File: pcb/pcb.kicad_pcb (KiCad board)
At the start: 2 copper layers, 61.6 x 63.7 mm, 7 parts, among them J1 Conn_01x02

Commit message: Reroute, repour
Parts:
- D1: footprint LED_SMD:LED_0805_2012Metric_Pad1.15x1.40mm_HandSolder -> pcb:universal_LED
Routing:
- net GND: track 144.9 -> 15.2 mm
- net +5V: track 131.2 -> 127.9 mm

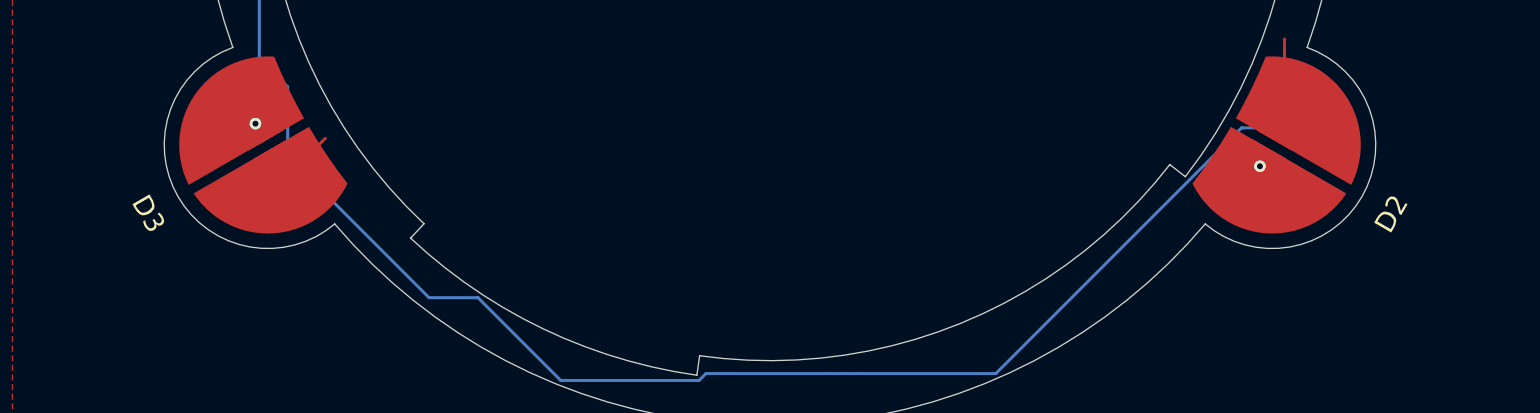
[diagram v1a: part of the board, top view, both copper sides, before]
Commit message: Update capitalization
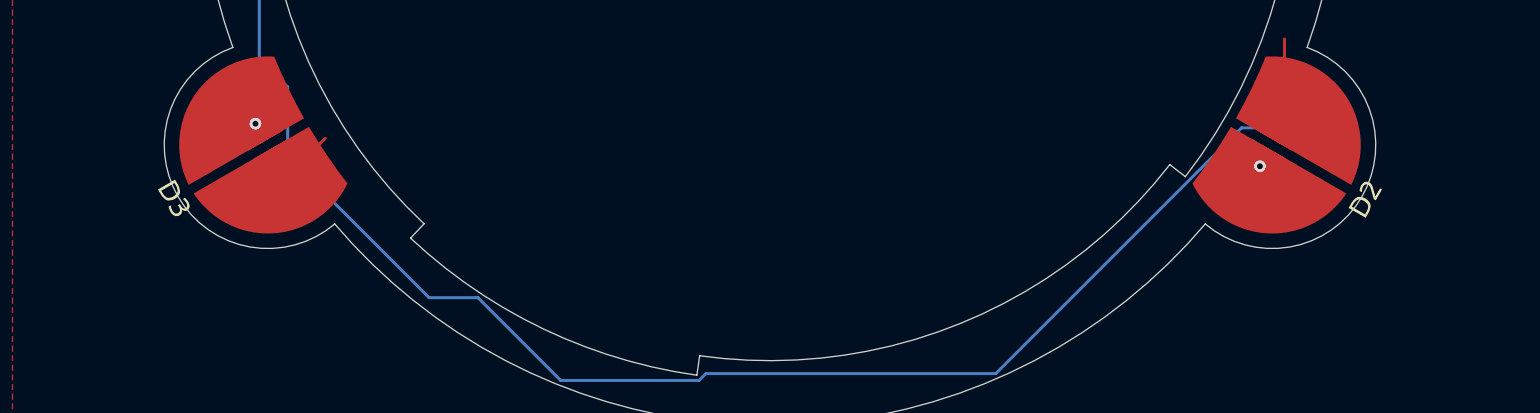
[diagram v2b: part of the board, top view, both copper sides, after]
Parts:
- D1, D2, D3: footprint pcb:universal_LED -> pcb:Universal_LED

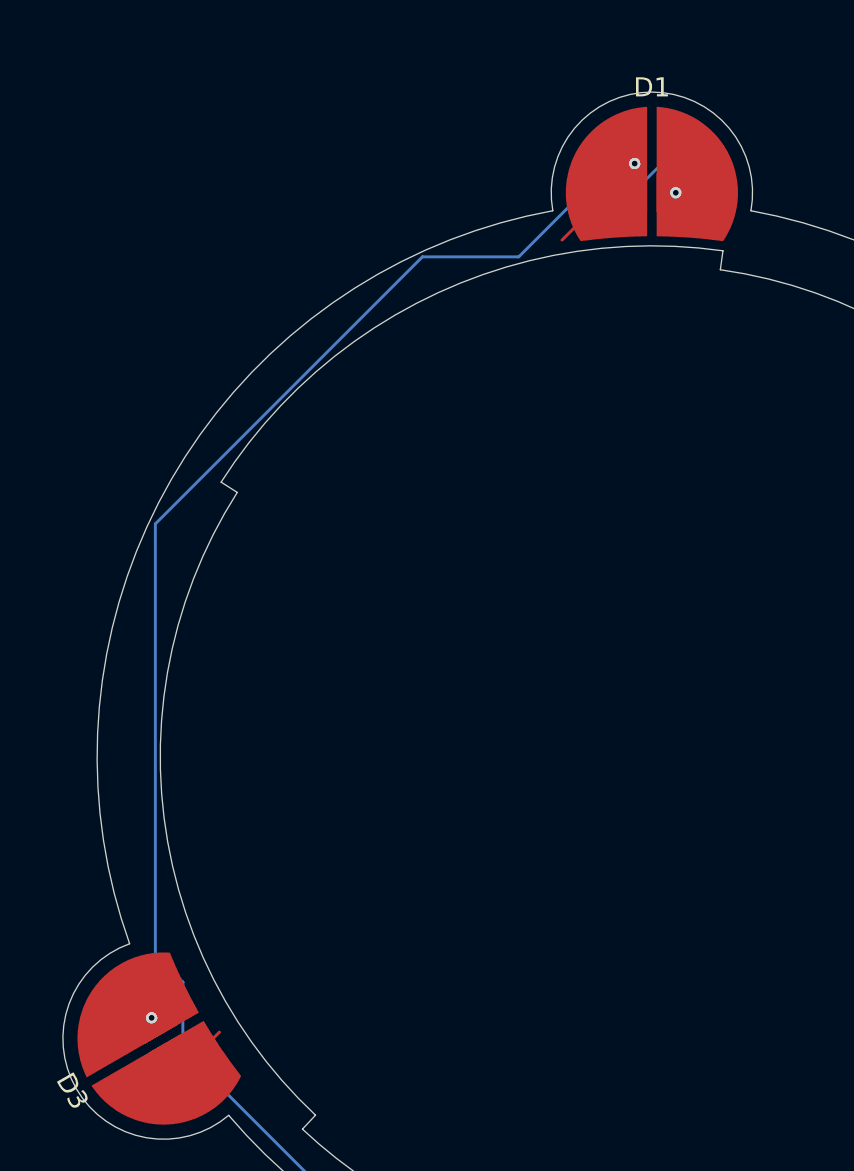
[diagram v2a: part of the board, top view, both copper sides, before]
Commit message: Use new power connection
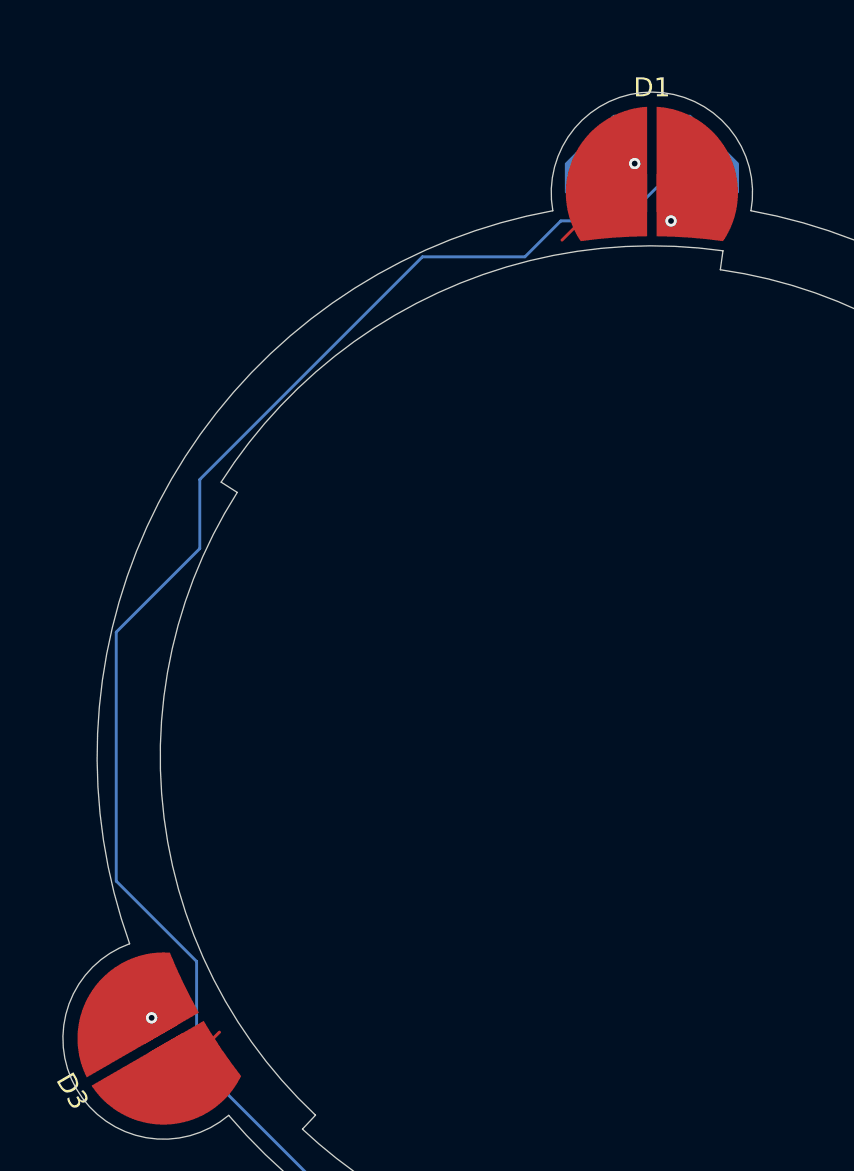
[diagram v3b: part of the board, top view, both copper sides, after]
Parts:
- J1: footprint Resistor_SMD:R_0805_2012Metric_Pad1.20x1.40mm_HandSolder -> pcb:Power_Connection
- moved J1 3.00 mm to (148.5, 75.5), turned to 180 degrees
- moved R1 1.47 mm to (148.5, 77.0)
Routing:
- net Net-(D1-Pad2): track 0.25 -> 1.80 mm
- net +5V: track 127.9 -> 129.1 mm
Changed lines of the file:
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@@
     (thickness 1.6)
     (drawings 18)
-    (tracks 38)
+    (tracks 42)
     (zones 0)
     (modules 7)
@@
     (38 B.Mask user hide)
     (39 F.Mask user hide)
-    (40 Dwgs.User user hide)
+    (40 Dwgs.User user)
     (41 Cmts.User user hide)
     (42 Eco1.User user hide)
@@
   )
   (module Resistor_SMD:R_0805_2012Metric_Pad1.20x1.40mm_HandSolder (layer B.Cu)
-    (at 148.5 72.5)
-    (descr "Resistor SMD 0805 (2012 Metric), square (rectangular) end terminal, IPC_7351 nominal with elongated pad for handsoldering. (Body size source: IPC-SM-782 page 72, https://www.pcb-3d.com/wordpress/wp-content/uploads/ipc-sm-782a_amendment_1_and_2.pdf), generated with kicad-footprint-generator")
-    (tags "resistor handsolder")
-    (attr smd)
-    (fp_text reference J1 (at 0 1.65 180) (layer B.SilkS)
-      (effects (font (size 1 1) (thickness 0.15)) (justify mirror))
-    )
-    (fp_text value Conn_01x02 (at 0 -1.65 180) (layer B.Fab)
-      (effects (font (size 1 1) (thickness 0.15)) (justify mirror))
-    )
-    (fp_text user %R (at 0 0 180) (layer B.Fab)
-      (effects (font (size 0.5 0.5) (thickness 0.08)) (justify mirror))
-    )
-    (fp_line (start -1 -0.625) (end -1 0.625) (layer B.Fab) (width 0.1))
-    (fp_line (start -1 0.625) (end 1 0.625) (layer B.Fab) (width 0.1))
-    (fp_line (start 1 0.625) (end 1 -0.625) (layer B.Fab) (width 0.1))
-    (fp_line (start 1 -0.625) (end -1 -0.625) (layer B.Fab) (width 0.1))
-    (fp_line (start -0.227064 0.735) (end 0.227064 0.735) (layer B.SilkS) (width 0.12))
-    (fp_line (start -0.227064 -0.735) (end 0.227064 -0.735) (layer B.SilkS) (width 0.12))
-    (fp_line (start -1.85 -0.95) (end -1.85 0.95) (layer B.CrtYd) (width 0.05))
-    (fp_line (start -1.85 0.95) (end 1.85 0.95) (layer B.CrtYd) (width 0.05))
-    (fp_line (start 1.85 0.95) (end 1.85 -0.95) (layer B.CrtYd) (width 0.05))
-    (fp_line (start 1.85 -0.95) (end -1.85 -0.95) (layer B.CrtYd) (width 0.05))
-    (pad 2 smd roundrect (at 1 0) (size 1.2 1.4) (layers B.Cu B.Paste B.Mask) (roundrect_rratio 0.208333)
-      (net 5 +5V))
-    (pad 1 smd roundrect (at -1 0) (size 1.2 1.4) (layers B.Cu B.Paste B.Mask) (roundrect_rratio 0.208333)
-      (net 2 GND))
-    (model ${KISYS3DMOD}/Resistor_SMD.3dshapes/R_0805_2012Metric.wrl
-      (at (xyz 0 0 0))
-      (scale (xyz 1 1 1))
-      (rotate (xyz 0 0 0))
-    )
-  )
-  (module Resistor_SMD:R_0805_2012Metric_Pad1.20x1.40mm_HandSolder (layer B.Cu)
     (at 122.975 119.737 300)
     (descr "Resistor SMD 0805 (2012 Metric), square (rectangular) end terminal, IPC_7351 nominal with elongated pad for handsoldering. (Body size source: IPC-SM-782 page 72, https://www.pcb-3d.com/wordpress/wp-content/uploads/ipc-sm-782a_amendment_1_and_2.pdf), generated with kicad-footprint-generator")
@@
   )
   (module Resistor_SMD:R_0805_2012Metric_Pad1.20x1.40mm_HandSolder (layer B.Cu)
-    (at 148.5 75.526)
+    (at 148.5 77)
     (descr "Resistor SMD 0805 (2012 Metric), square (rectangular) end terminal, IPC_7351 nominal with elongated pad for handsoldering. (Body size source: IPC-SM-782 page 72, https://www.pcb-3d.com/wordpress/wp-content/uploads/ipc-sm-782a_amendment_1_and_2.pdf), generated with kicad-footprint-generator")
     (tags "resistor handsolder")
@@
       ))
   )
+  (module pcb:Power_Connection (layer B.Cu)
+    (at 148.5 75.5 180)
+    (fp_text reference J1 (at 0 5) (layer B.SilkS)
+      (effects (font (size 1 1) (thickness 0.15)) (justify mirror))
+    )
+    (fp_text value Conn_01x02 (at 0 -1) (layer B.Fab)
+      (effects (font (size 1 1) (thickness 0.15)) (justify mirror))
+    )
+    (pad 1 smd custom (at 1.5 1.5 180) (size 2 2) (layers B.Cu B.Paste B.Mask)
+      (net 2 GND) (zone_connect 0)
+      (options (clearance outline) (anchor rect))
+      (primitives
+        (gr_poly (pts
+           (xy 3 0) (xy 3 -1.5) (xy -1 -1.5) (xy -1 2.5) (xy 0.5 2.5)
+) (width 0.1))
+      ))
+    (pad 2 smd custom (at -1.5 1.5 180) (size 2 2) (layers B.Cu B.Paste B.Mask)
+      (net 5 +5V) (zone_connect 0)
+      (options (clearance outline) (anchor rect))
+      (primitives
+        (gr_poly (pts
+           (xy -0.5 2.5) (xy 1 2.5) (xy 1 -1.5) (xy -3 -1.5) (xy -3 0)
+) (width 0.1))
+      ))
+  )
   (gr_arc (start 148.5 104.999999) (end 143.321428 76.466118) (angle -99.42687878) (layer Edge.Cuts) (width 0.05))
   (gr_arc (start 122.974998 119.736866) (end 121.199647 114.782166) (angle -200.5731212) (layer Edge.Cuts) (width 0.05))
@@
   (gr_arc (start 148.5 104.999999) (end 169.610346 121.347577) (angle -62.77165651) (layer Edge.Cuts) (width 0.05))
   (gr_line (start 171.788711 94.131425) (end 172.694887 93.708523) (layer Edge.Cuts) (width 0.05))
+  (segment (start 149.75 75.526) (end 149.974 75.526) (width 0.1524) (layer F.Cu) (net 1))
+  (via (at 149.5 77) (size 0.6) (drill 0.3) (layers F.Cu B.Cu) (net 1))
+  (segment (start 149.75 76.75) (end 149.5 77) (width 0.1524) (layer F.Cu) (net 1))
+  (segment (start 149.75 75.526) (end 149.75 76.75) (width 0.1524) (layer F.Cu) (net 1))
   (via (at 147.6 74) (size 0.6) (drill 0.3) (layers F.Cu B.Cu) (net 2))
-  (via (at 149.75 75.526) (size 0.6) (drill 0.3) (layers F.Cu B.Cu) (net 1))
-  (segment (start 149.5 75.526) (end 149.75 75.526) (width 0.1524) (layer B.Cu) (net 1))
   (segment (start 174.65 118.654468) (end 174.65 114.35) (width 0.1524) (layer F.Cu) (net 2))
   (segment (start 123.6 120.819532) (end 124.480468 120.819532) (width 0.1524) (layer F.Cu) (net 2))
@@
   (segment (start 122.475 118.779468) (end 122.35 118.654468) (width 0.1524) (layer B.Cu) (net 4))
   (segment (start 122.475 118.870975) (end 122.475 118.779468) (width 0.1524) (layer B.Cu) (net 4))
-  (segment (start 149.5 73.526) (end 147.5 75.526) (width 0.1524) (layer B.Cu) (net 5))
   (segment (start 149.5 72.5) (end 149.5 73.526) (width 0.1524) (layer B.Cu) (net 5))
   (segment (start 173.838129 118.870975) (end 174.525 118.870975) (width 0.1524) (layer B.Cu) (net 5))
@@
   (segment (start 174.525 118.870975) (end 172.46148 118.870975) (width 0.1524) (layer B.Cu) (net 5))
   (segment (start 123.475 120.603025) (end 124.7 119.378025) (width 0.1524) (layer B.Cu) (net 5))
-  (segment (start 136.503807 78.876854) (end 141.540816 78.876854) (width 0.1524) (layer B.Cu) (net 5))
-  (segment (start 122.545585 92.835076) (end 136.503807 78.876854) (width 0.1524) (layer B.Cu) (net 5))
-  (segment (start 122.545585 115.348258) (end 122.545585 92.835076) (width 0.1524) (layer B.Cu) (net 5))
-  (segment (start 123.987435 116.790108) (end 122.545585 115.348258) (width 0.1524) (layer B.Cu) (net 5))
-  (segment (start 123.987435 120.09059) (end 123.987435 116.790108) (width 0.1524) (layer B.Cu) (net 5))
-  (segment (start 123.475 120.603025) (end 123.987435 120.09059) (width 0.1524) (layer B.Cu) (net 5))
-  (segment (start 144.89167 75.526) (end 147.5 75.526) (width 0.1524) (layer B.Cu) (net 5))
-  (segment (start 141.540816 78.876854) (end 144.89167 75.526) (width 0.1524) (layer B.Cu) (net 5))
+  (segment (start 147.5 76.5) (end 147.5 77) (width 0.1524) (layer B.Cu) (net 5))
+  (segment (start 150 74) (end 147.5 76.5) (width 0.1524) (layer B.Cu) (net 5))
+  (segment (start 143.739662 77) (end 147.5 77) (width 0.1524) (layer B.Cu) (net 5))
+  (segment (start 136.503807 78.876854) (end 141.862808 78.876854) (width 0.1524) (layer B.Cu) (net 5))
+  (segment (start 141.862808 78.876854) (end 143.739662 77) (width 0.1524) (layer B.Cu) (net 5))
+  (segment (start 124.86706 90.513601) (end 136.503807 78.876854) (width 0.1524) (layer B.Cu) (net 5))
+  (segment (start 124.86706 94.12619) (end 124.86706 90.513601) (width 0.1524) (layer B.Cu) (net 5))
+  (segment (start 120.5 98.49325) (end 124.86706 94.12619) (width 0.1524) (layer B.Cu) (net 5))
+  (segment (start 120.5 111.507054) (end 120.5 98.49325) (width 0.1524) (layer B.Cu) (net 5))
+  (segment (start 124.7 115.707054) (end 120.5 111.507054) (width 0.1524) (layer B.Cu) (net 5))
+  (segment (start 124.7 119.378025) (end 124.7 115.707054) (width 0.1524) (layer B.Cu) (net 5))
   (zone (net 2) (net_name GND) (layer F.Cu) (hatch edge 0.508)
     (connect_pads (clearance 0.1524))
